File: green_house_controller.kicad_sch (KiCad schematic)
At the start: 10 parts, among them J2 Screw_Terminal_01x10, J3 USB_B_Mini, J4 Screw_Terminal_01x06, J5 Screw_Terminal_01x03, J6 Barrel_Jack, U8 DHT11

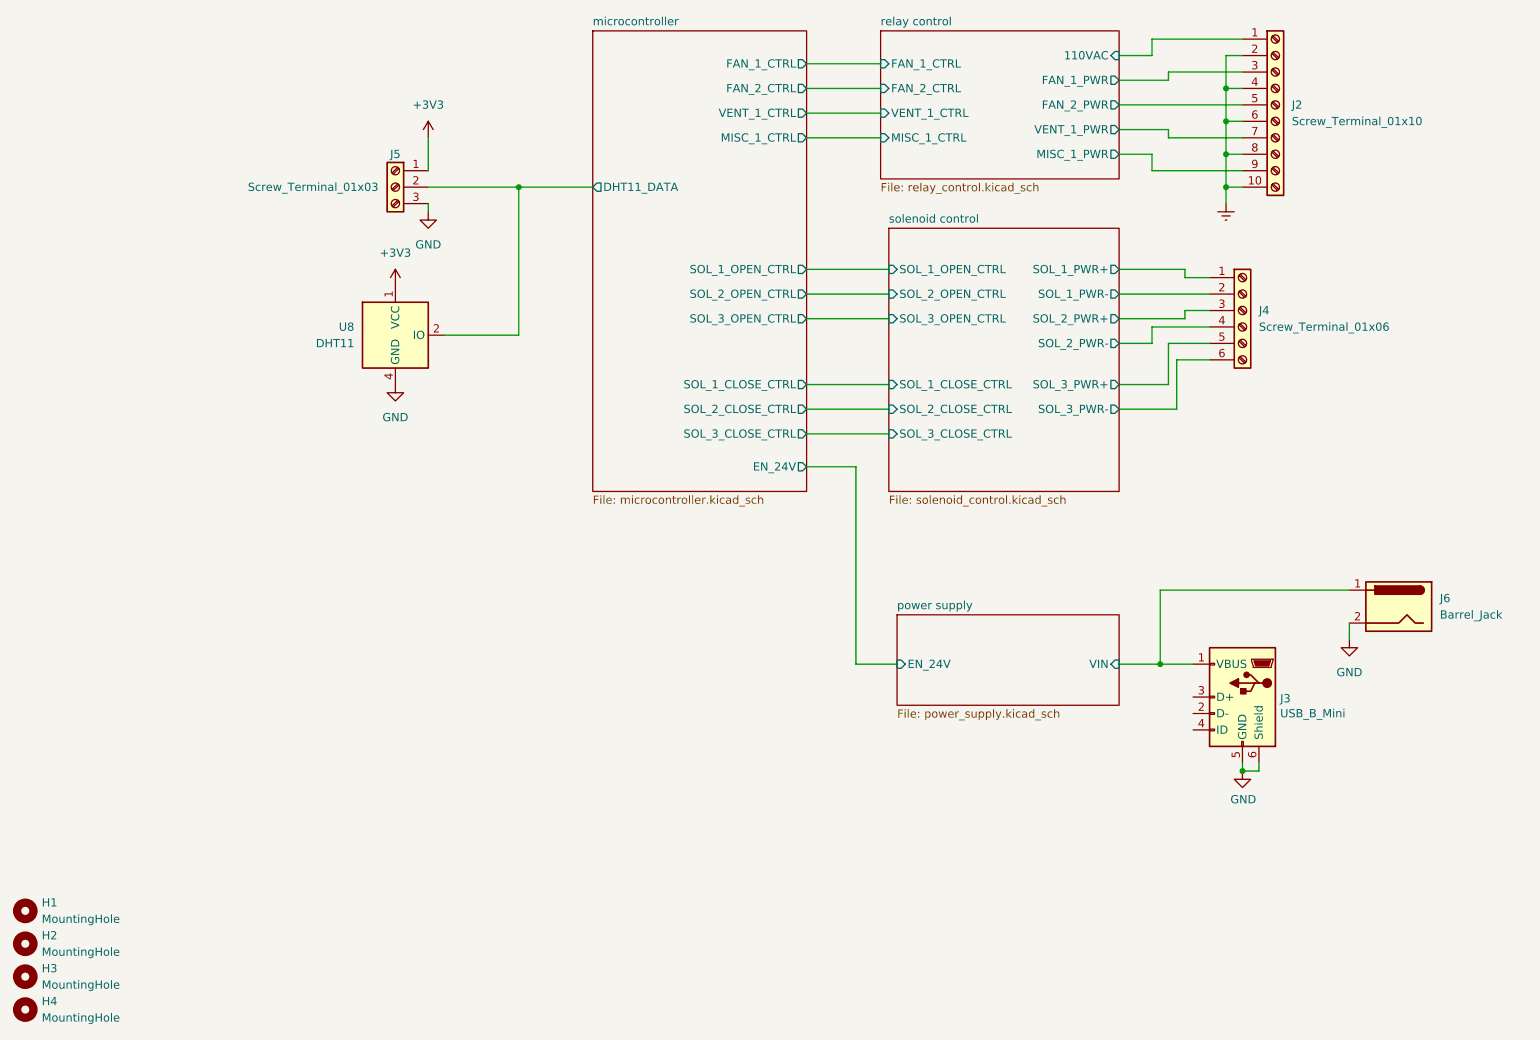
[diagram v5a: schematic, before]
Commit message: Replaced relays with smd versions.
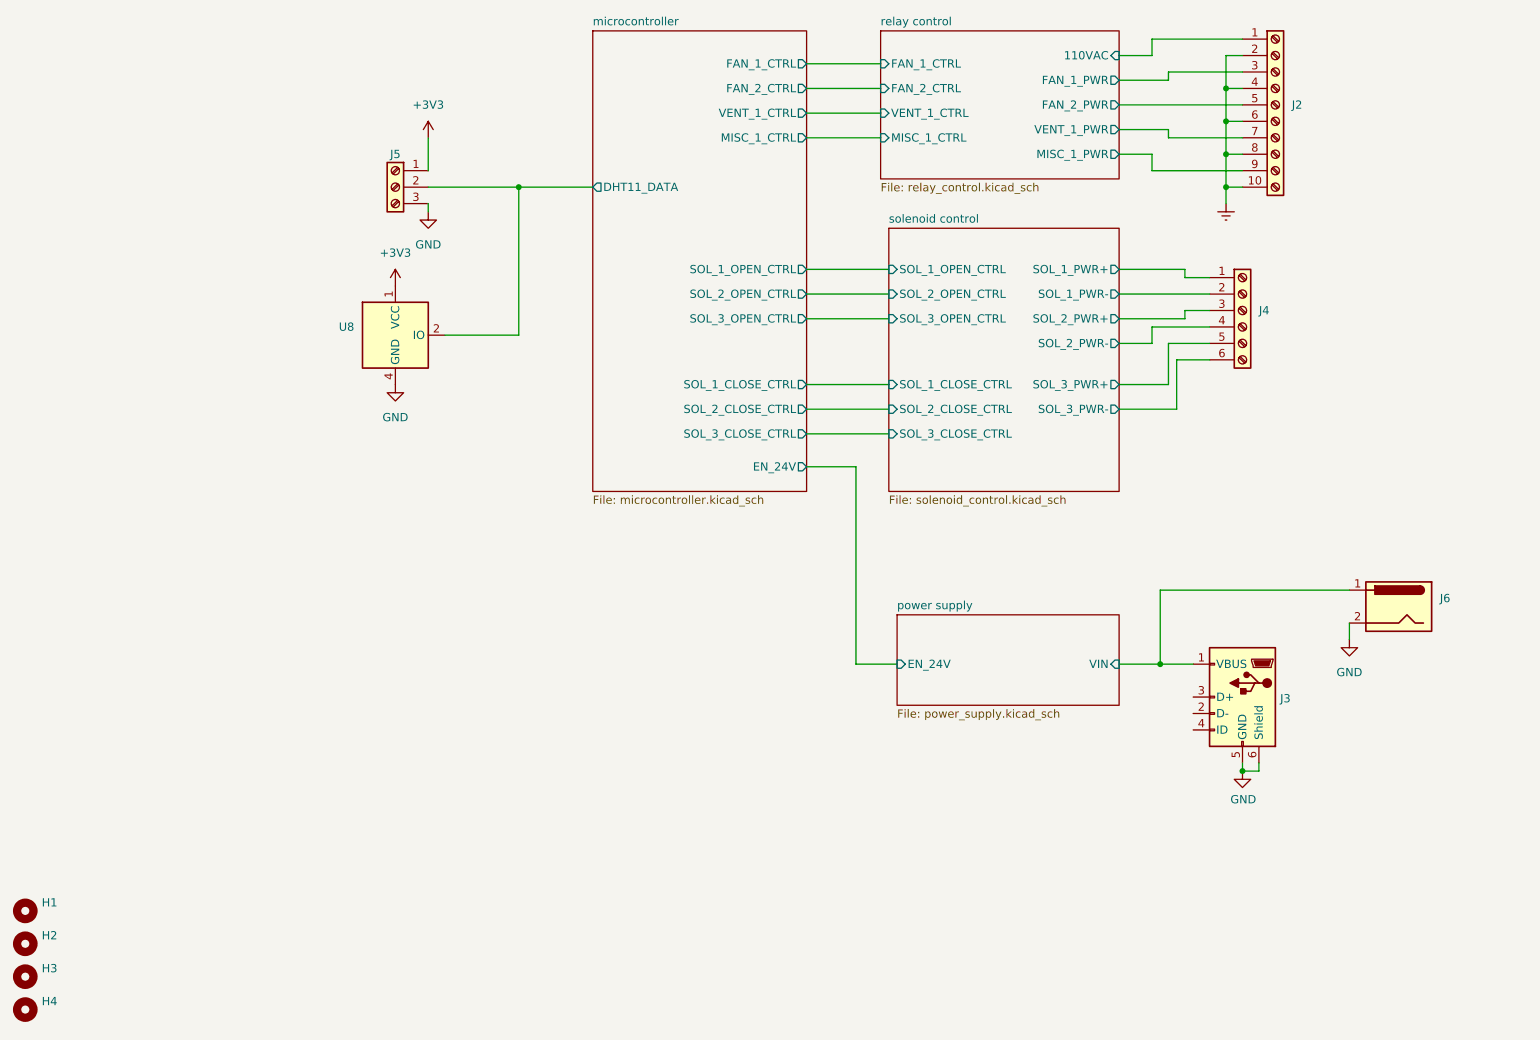
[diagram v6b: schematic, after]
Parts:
- H1, H2, H3, H4: value MountingHole -> (none); footprint MountingHole:MountingHole_3.2mm_M3 -> (none)
- J2: value Screw_Terminal_01x10 -> (none); footprint Connector_Phoenix_MC_HighVoltage:PhoenixContact_MCV_1,5_10-G-5.08_1x10_P5.08mm_Vertical -> (none)
- J3: value USB_B_Mini -> (none); footprint Connector_USB:USB_Mini-B_Lumberg_2486_01_Horizontal -> (none)
- J4: value Screw_Terminal_01x06 -> (none); footprint Connector_Phoenix_MC_HighVoltage:PhoenixContact_MCV_1,5_6-G-5.08_1x06_P5.08mm_Vertical -> (none)
- J5: value Screw_Terminal_01x03 -> (none); footprint Connector_Phoenix_MC_HighVoltage:PhoenixContact_MCV_1,5_3-G-5.08_1x03_P5.08mm_Vertical -> (none)
- J6: value Barrel_Jack -> (none); footprint Connector_BarrelJack:BarrelJack_CUI_PJ-102AH_Horizontal -> (none)
- U8: value DHT11 -> (none); footprint Sensor:Aosong_DHT11_5.5x12.0_P2.54mm -> (none)
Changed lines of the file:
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@@
       (effects (font (size 1.27 1.27)) (justify right))
     )
-    (property "Value" "USB_B_Mini" (id 1) (at 212.8266 147.32 0)
-      (effects (font (size 1.27 1.27)) (justify right))
-    )
-    (property "Footprint" "Connector_USB:USB_Mini-B_Lumberg_2486_01_Horizontal" (id 2) (at 203.2 146.05 0)
+    (property "Value" "" (id 1) (at 212.8266 147.32 0)
+      (effects (font (size 1.27 1.27)) (justify right))
+    )
+    (property "Footprint" "" (id 2) (at 203.2 146.05 0)
       (effects (font (size 1.27 1.27)) hide)
     )
@@
       (effects (font (size 1.27 1.27)) (justify left))
     )
-    (property "Value" "Screw_Terminal_01x10" (id 1) (at 214.63 55.8799 0)
-      (effects (font (size 1.27 1.27)) (justify left))
-    )
-    (property "Footprint" "Connector_Phoenix_MC_HighVoltage:PhoenixContact_MCV_1,5_10-G-5.08_1x10_P5.08mm_Vertical" (id 2) (at 212.09 53.34 0)
+    (property "Value" "" (id 1) (at 214.63 55.8799 0)
+      (effects (font (size 1.27 1.27)) (justify left))
+    )
+    (property "Footprint" "" (id 2) (at 212.09 53.34 0)
       (effects (font (size 1.27 1.27)) hide)
     )
@@
       (effects (font (size 1.27 1.27)) (justify left))
     )
-    (property "Value" "MountingHole" (id 1) (at 21.59 194.3099 0)
-      (effects (font (size 1.27 1.27)) (justify left))
-    )
-    (property "Footprint" "MountingHole:MountingHole_3.2mm_M3" (id 2) (at 19.05 193.04 0)
+    (property "Value" "" (id 1) (at 21.59 194.3099 0)
+      (effects (font (size 1.27 1.27)) (justify left))
+    )
+    (property "Footprint" "" (id 2) (at 19.05 193.04 0)
       (effects (font (size 1.27 1.27)) hide)
     )
@@
       (effects (font (size 1.27 1.27)) (justify right))
     )
-    (property "Value" "Barrel_Jack" (id 1) (at 237.49 132.0799 0)
-      (effects (font (size 1.27 1.27)) (justify right))
-    )
-    (property "Footprint" "Connector_BarrelJack:BarrelJack_CUI_PJ-102AH_Horizontal" (id 2) (at 229.87 131.826 0)
+    (property "Value" "" (id 1) (at 237.49 132.0799 0)
+      (effects (font (size 1.27 1.27)) (justify right))
+    )
+    (property "Footprint" "" (id 2) (at 229.87 131.826 0)
       (effects (font (size 1.27 1.27)) hide)
     )
@@
       (effects (font (size 1.27 1.27)) (justify left))
     )
-    (property "Value" "MountingHole" (id 1) (at 21.59 184.1499 0)
-      (effects (font (size 1.27 1.27)) (justify left))
-    )
-    (property "Footprint" "MountingHole:MountingHole_3.2mm_M3" (id 2) (at 19.05 182.88 0)
+    (property "Value" "" (id 1) (at 21.59 184.1499 0)
+      (effects (font (size 1.27 1.27)) (justify left))
+    )
+    (property "Footprint" "" (id 2) (at 19.05 182.88 0)
       (effects (font (size 1.27 1.27)) hide)
     )
@@
       (effects (font (size 1.27 1.27)) (justify left))
     )
-    (property "Value" "MountingHole" (id 1) (at 21.59 179.0699 0)
-      (effects (font (size 1.27 1.27)) (justify left))
-    )
-    (property "Footprint" "MountingHole:MountingHole_3.2mm_M3" (id 2) (at 19.05 177.8 0)
+    (property "Value" "" (id 1) (at 21.59 179.0699 0)
+      (effects (font (size 1.27 1.27)) (justify left))
+    )
+    (property "Footprint" "" (id 2) (at 19.05 177.8 0)
       (effects (font (size 1.27 1.27)) hide)
     )
@@
       (effects (font (size 1.27 1.27)) (justify right))
     )
-    (property "Value" "DHT11" (id 1) (at 69.85 90.1699 0)
-      (effects (font (size 1.27 1.27)) (justify right))
-    )
-    (property "Footprint" "Sensor:Aosong_DHT11_5.5x12.0_P2.54mm" (id 2) (at 76.2 99.06 0)
+    (property "Value" "" (id 1) (at 69.85 90.1699 0)
+      (effects (font (size 1.27 1.27)) (justify right))
+    )
+    (property "Footprint" "" (id 2) (at 76.2 99.06 0)
       (effects (font (size 1.27 1.27)) hide)
     )
@@
       (effects (font (size 1.27 1.27)) (justify left))
     )
-    (property "Value" "Screw_Terminal_01x06" (id 1) (at 209.55 87.6299 0)
-      (effects (font (size 1.27 1.27)) (justify left))
-    )
-    (property "Footprint" "Connector_Phoenix_MC_HighVoltage:PhoenixContact_MCV_1,5_6-G-5.08_1x06_P5.08mm_Vertical" (id 2) (at 207.01 85.09 0)
+    (property "Value" "" (id 1) (at 209.55 87.6299 0)
+      (effects (font (size 1.27 1.27)) (justify left))
+    )
+    (property "Footprint" "" (id 2) (at 207.01 85.09 0)
       (effects (font (size 1.27 1.27)) hide)
     )
@@
     (in_bom yes) (on_board yes)
     (property "Reference" "J5" (id 0) (at 76.2 60.96 0))
-    (property "Value" "Screw_Terminal_01x03" (id 1) (at 63.5 66.04 0))
-    (property "Footprint" "Connector_Phoenix_MC_HighVoltage:PhoenixContact_MCV_1,5_3-G-5.08_1x03_P5.08mm_Vertical" (id 2) (at 76.2 66.04 0)
+    (property "Value" "" (id 1) (at 63.5 66.04 0))
+    (property "Footprint" "" (id 2) (at 76.2 66.04 0)
       (effects (font (size 1.27 1.27)) hide)
     )
@@
       (effects (font (size 1.27 1.27)) (justify left))
     )
-    (property "Value" "MountingHole" (id 1) (at 21.59 189.2299 0)
-      (effects (font (size 1.27 1.27)) (justify left))
-    )
-    (property "Footprint" "MountingHole:MountingHole_3.2mm_M3" (id 2) (at 19.05 187.96 0)
+    (property "Value" "" (id 1) (at 21.59 189.2299 0)
+      (effects (font (size 1.27 1.27)) (justify left))
+    )
+    (property "Footprint" "" (id 2) (at 19.05 187.96 0)
       (effects (font (size 1.27 1.27)) hide)
     )
@@
     )
     (path "/00000000-0000-0000-0000-0000625b126e/00000000-0000-0000-0000-0000625b6c1d"
-      (reference "C2") (unit 1) (value "20uF") (footprint "Capacitor_SMD:C_0805_2012Metric")
+      (reference "C2") (unit 1) (value "10uF") (footprint "Capacitor_SMD:C_0805_2012Metric")
     )
     (path "/00000000-0000-0000-0000-0000625b126e/00000000-0000-0000-0000-0000625b8a08"
@@
     )
     (path "/00000000-0000-0000-0000-0000626492a4/87535086-737b-49ec-86b0-9f512f7dc309"
-      (reference "U3") (unit 1) (value "TLP3825TP1_F") (footprint "Package_DIP:DIP-8_W7.62mm")
+      (reference "U3") (unit 1) (value "TLP3825TP1_F") (footprint "Package_DIP:DIP-8_W7.62mm_SMDSocket_SmallPads")
     )
     (path "/00000000-0000-0000-0000-0000626492a4/7857de86-00ae-4515-9772-2a946a58e571"
-      (reference "U4") (unit 1) (value "TLP3825TP1_F") (footprint "Package_DIP:DIP-8_W7.62mm")
+      (reference "U4") (unit 1) (value "TLP3825TP1_F") (footprint "Package_DIP:DIP-8_W7.62mm_SMDSocket_SmallPads")
     )
     (path "/00000000-0000-0000-0000-0000626492a4/de15d44b-3992-4da4-8503-c5ddb6928473"
-      (reference "U5") (unit 1) (value "TLP3825TP1_F") (footprint "Package_DIP:DIP-8_W7.62mm")
+      (reference "U5") (unit 1) (value "TLP3825TP1_F") (footprint "Package_DIP:DIP-8_W7.62mm_SMDSocket_SmallPads")
     )
     (path "/00000000-0000-0000-0000-0000626492a4/a6849e79-c2c5-4768-b505-16141e6d58f9"
-      (reference "U6") (unit 1) (value "TLP3825TP1_F") (footprint "Package_DIP:DIP-8_W7.62mm")
+      (reference "U6") (unit 1) (value "TLP3825TP1_F") (footprint "Package_DIP:DIP-8_W7.62mm_SMDSocket_SmallPads")
     )
     (path "/00000000-0000-0000-0000-0000625b57c4/ac210a49-c24d-4806-9928-7d16f18214ee"
